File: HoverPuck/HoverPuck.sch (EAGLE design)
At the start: 14 parts, among them Q1 FDME, Q2 FDME, U1 EFM8BB1.QFN20, U2 TPS62177.DQC

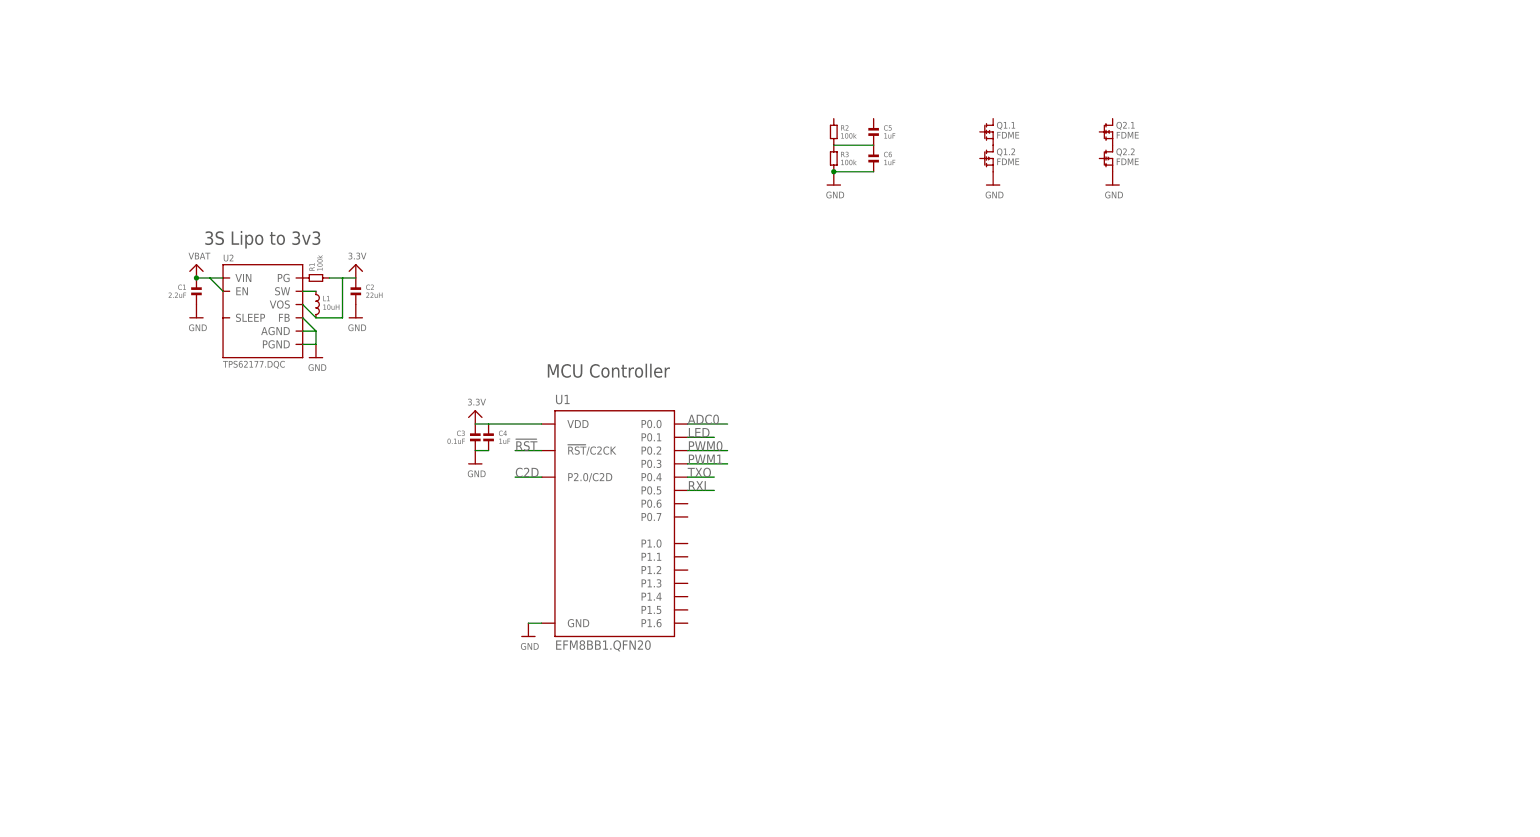
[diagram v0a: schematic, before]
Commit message: Schematic seems about done and layout of components looks promising Next step will be the actual routing
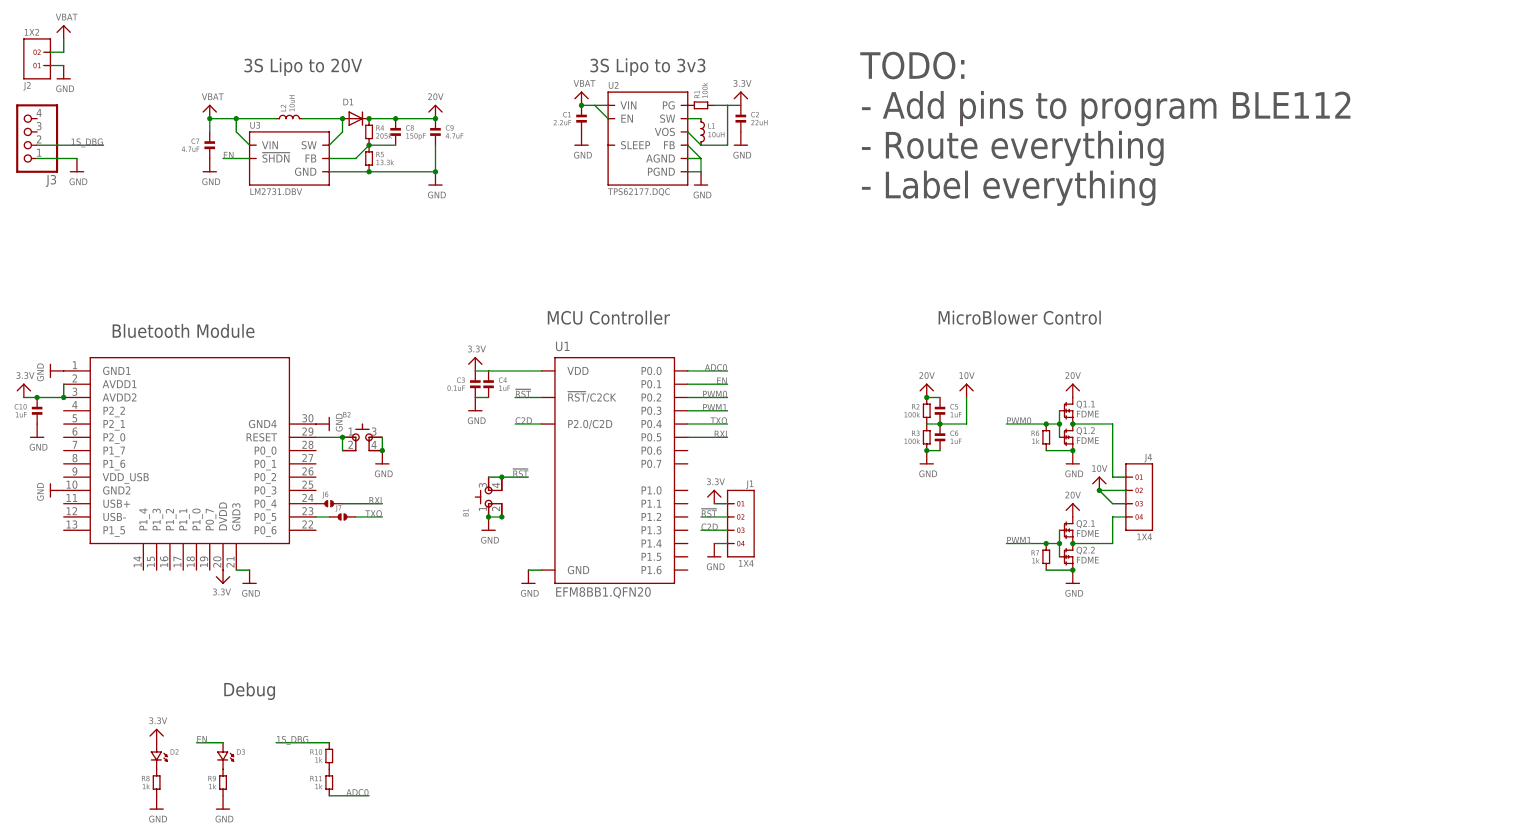
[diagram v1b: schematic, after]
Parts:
- added B1, B2: (no value), alps:SKSCLDE010
- added C10: 1uF, standardparts:CAPACITOR.0603
- added C7, C9: 4.7uF, standardparts:CAPACITOR.0805
- added C8: 150pF, standardparts:CAPACITOR.0603
- added D1: MBR0530T1G, microbuilder:DIODESOD-123
- added D2, D3: (no value), standardparts:LED.0603
- added J1, J4: 1X4, headers(2mm):1X4
- added J2: 1X2, headers.edge(.1in):1X2
- added J3: (no value), microbuilder:JST_4PIN
- added J6, J7: (no value), solderjumper:SOLDERJUMPER.2.SML.PASTE
- added L2: 10uH, bourns:INDUCTOR-SRN6045
- added R10, R11, R6, R7, R8, R9: 1k, standardparts:RESISTOR.0603
- added R4: 205k, standardparts:RESISTOR.0603
- added R5: 13.3k, standardparts:RESISTOR.0603
- added U3: LM2731.DBV, packages(ti):LM2731.DBV
- added U4: BLE112-A, SparkFun-RF:BLE112-A
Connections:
- removed net LED: U1.P0.1
- new net 10V: C5.2, C6.1, J4.2, J4.3, R2.2, R3.1
- new net 1S_DBG: J3.2, R10.1
- new net 20V: C5.1, C8.1, C9.1, D1.C, Q1.1.D, Q2.1.D, R2.1, R4.1
- new net EN: D2.1, D3.1, U1.P0.1, U3.!SHDN
- new net N$10: J6.1, U4.P0_4
- new net N$11: J7.1, U4.P0_5
- new net N$12: B2.1, B2.2, U4.RESET
- new net N$5: D1.A, L2.2, U3.SW
- new net N$7: C8.2, R4.2, R5.1, U3.FB
- new net N$8: D3.2, R9.1
- new net N$9: R10.2, R11.1
- net !RST: now also B1.3, B1.4, J1.2
- net 3.3V: now also C10.1, J1.1, U4.AVDD1, U4.AVDD2, U4.DVDD
- net ADC0: now also R11.2
- net C2D: now also J1.3
- net GND: now also B1.1, B1.2, B2.3, B2.4, C10.2, C7.2, C9.2, J1.4, J2.1, J3.1, R5.2, R6.2, R7.2, R8.2, R9.2, U3.GND, U4.GND1, U4.GND2, U4.GND3, U4.GND4
- net N$1: now also J4.1
- net N$2: now also J4.4
- net N$4: now also D2.2, R8.1; no longer C5.2, C6.1, R2.2, R3.1
- net PWM0: now also Q1.1.G, Q1.2.G, R6.1
- net PWM1: now also Q2.1.G, Q2.2.G, R7.1
- net RXI: now also J6.2
- net TXO: now also J7.2
- net VBAT: now also C7.1, J2.2, L2.1, U3.VIN
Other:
- note added: "3S Lipo to 20V"
- note added: "Bluetooth Module"
- note added: "Debug"
- note added: "MicroBlower Control"
- note added: "TODO: - Add pins to program BLE112 - Route everything - Label everything"
- moved on the sheet: C1, C2, C3, C4, C5, C6, L1, Q1.1, Q1.2, Q2.1, Q2.2, R1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

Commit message: Updated TODO list
Added more references on what signals to breakout for BLE112
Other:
- note added: "TODO: - Add pins to program BLE112 - Finish Routing - Label everything - Breakout Programming pins for BLE112 - https://github.com/slackhappy/ble112/blob/master/programming.md - http://www.inmojo.com/store/jeff-rowberg/item/ble112-bluetooth-low-energy-breakout/ - https://github.com/slackhappy/ble112/tree/master/serial_debug - Breakout Programming pins for EFM8BB1 - -"
- note removed: "TODO: - Add pins to program BLE112 - Route everything - Label everything"
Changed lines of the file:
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@@
 <text x="170.18" y="165.1" size="5.08" layer="97" ratio="15" align="top-left">TODO:
 - Add pins to program BLE112
-- Route everything
-- Label everything</text>
+- Finish Routing
+- Label everything
+- Breakout Programming pins for BLE112
+  - https://github.com/slackhappy/ble112/blob/master/programming.md
+  - http://www.inmojo.com/store/jeff-rowberg/item/ble112-bluetooth-low-energy-breakout/
+  - https://github.com/slackhappy/ble112/tree/master/serial_debug
+- Breakout Programming pins for EFM8BB1
+  -
+- </text>
 <text x="200.66" y="114.3" size="2.54" layer="97" ratio="15" align="center">MicroBlower Control</text>
 <text x="53.34" y="43.18" size="2.54" layer="97" ratio="15" align="center">Debug</text>

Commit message: Added single debugger connector
Replaced 1k resistors with resistor array
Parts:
- removed B2: (no value), alps:SKSCLDE010
- removed J1: 1X4, headers(2mm):1X4
- removed R8, R9: 1k, standardparts:RESISTOR.0603
- added D4: (no value), standardparts:LED.0603
- added RA1: (no value), resistorarray:RA-4.0603
- added U$38, U$39: 1X5, headers(.05in):1X5
- R10, R11, R6, R7: value 1k -> 10k
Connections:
- removed net !RST: B1.3, B1.4, J1.2, U1.!RST!/C2CK
- removed net C2D: J1.3, U1.P2.0/C2D
- removed net EN: D2.1, D3.1, U1.P0.1, U3.!SHDN
- removed net N$12: B2.1, B2.2, U4.RESET
- new net 20V_EN: RA1.2.2, U1.P0.1, U3.!SHDN
- new net BLE_!RST: RA1.4.1, U$38.4, U1.P0.7, U4.RESET
- new net BLE_DC: U$38.2, U4.P2_2
- new net BLE_DD: U$39.2, U4.P2_1
- new net EFM8_C2CK: B1.3, B1.4, U$39.3, U1.!RST!/C2CK
- new net EFM8_C2D: U$38.3, U1.P2.0/C2D
- new net STATUS: RA1.3.2, U1.P0.6
- net 3.3V: now also RA1.1.2, RA1.4.2, U$38.5, U$39.1; no longer J1.1
- net ADC0: now also R10.2, R11.1; no longer R11.2
- net GND: now also D2.2, D3.2, D4.2, R11.2, U$38.1, U$39.5; no longer B2.3, B2.4, J1.4, R8.2, R9.2
- net N$4: now also D2.1, RA1.1.1; no longer D2.2, R8.1
- net N$8: now also D3.1, RA1.2.1; no longer D3.2, R9.1
- net N$9: now also D4.1, RA1.3.1; no longer R10.2, R11.1
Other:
- note added: "TODO: - Optimize pin placement in EFM8 - Add testpoints everywhere - Complete routing"
- note removed: "TODO: - Add pins to program BLE112 - Finish Routing - Label everything - Breakout Programming pins for BLE112 - https://github.com/slackhappy/ble112/blob/master/programming.md - http://www.inmojo.com/store/jeff-rowberg/item/ble112-bluetooth-low-energy-breakout/ - https://github.com/slackhappy/ble112/tree/master/serial_debug - Breakout Programming pins for EFM8BB1 - -"
- moved on the sheet: B1, C10, C3, C4, C5, C6, D2, D3, J4, J6, J7, Q1.1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

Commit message: Completed v1 of HoverPuck PCB
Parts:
- added J1: (no value), solderjumper:SOLDERJUMPER.2.SML.PASTE
- added TP1, TP2, TP3, TP4: TPTP06R, testpad:TPTP06R
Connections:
- removed net N$9 (its old number): D4.1, RA1.3.1
- new net N$12: J1.1, U1.P0.1
- new net N$8: D4.1, RA1.1.1
- net 20V: now also TP2.TP
- net 20V_EN: now also U1.P0.0; no longer U1.P0.1
- net 3.3V: now also RA1.3.2, TP1.TP; no longer RA1.1.2
- net ADC0: now also J1.2; no longer U1.P0.0
- net BLE_!RST: now also RA1.3.1, U1.P1.0; no longer RA1.4.1, U1.P0.7
- net N$4: now also RA1.4.1; no longer RA1.1.1
- net PWM0: now also Q2.1.G, Q2.2.G, R7.1, TP4.TP, U1.P0.3; no longer Q1.1.G, Q1.2.G, R6.1, U1.P0.2
- net PWM1: now also Q1.1.G, Q1.2.G, R6.1, TP3.TP, U1.P0.6; no longer Q2.1.G, Q2.2.G, R7.1, U1.P0.3
- net STATUS: now also RA1.1.2, U1.P0.7; no longer RA1.3.2, U1.P0.6
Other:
- note added: "AnomalousMaker.com"
- note added: "Author: Cruz Monrreal II"
- note removed: "TODO: - Optimize pin placement in EFM8 - Add testpoints everywhere - Complete routing"
- moved on the sheet: C2, RA1.1, RA1.3, RA1.4

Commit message: Started v2 of the HoverPuck. Changed driver circuit, and moving things around. New driver circuit still needs to be confirmed functional.
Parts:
- removed J3: (no value), microbuilder:JST_4PIN
- removed J4: 1X4, headers(2mm):1X4
- removed Q1, Q2: FDME, fairchild:FDME
- removed R2, R3: 100k, standardparts:RESISTOR.0603
- removed R6, R7: 10k, standardparts:RESISTOR.0603
- added C11, C12, C13, C14: 0.1uF, standardparts:CAPACITOR.0603
- added MB0, MB1: 1X2, headers.edge(.1in):1X2
- added TP5, TP6: TPTP06R, testpad:TPTP06R
- added U5, U6: (no value), packages(ti):DRV8800.RTY
- C5, C6: value 1uF -> 0.1uF
- J2: value 1X2 -> 1X4; device headers.edge(.1in):1X2 -> headers.edge(.1in):1X4
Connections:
- removed net 10V: C5.2, C6.1, J4.2, J4.3, R2.2, R3.1
- new net 12V: C12.1, C13.1, C14.1, C5.1, U5.VMOT, U6.VMOT
- new net EN_20V: U5.!SLEEP, U6.!SLEEP
- new net N$13: MB0.1, U5.OUT+
- new net N$14: MB0.2, U5.OUT-
- new net N$15: MB1.1, U6.OUT+
- new net N$16: MB1.2, U6.OUT-
- new net N$17: C6.1, U5.CP1
- new net N$18: C6.2, U5.CP2
- new net N$19: C11.2, U6.CP2
- new net N$20: C11.1, U6.CP1
- net 1S_DBG: now also J2.3; no longer J3.2
- net 20V: no longer C5.1, Q1.1.D, Q2.1.D, R2.1
- net 20V_EN: now also TP5.TP
- net 3.3V: now also U5.ENABLE, U5.MODE, U6.ENABLE, U6.MODE
- net GND: now also C13.2, C14.2, J2.4, TP6.TP, U5.GND, U5.SENSE, U6.GND, U6.SENSE; no longer C6.2, J2.1, J3.1, Q1.2.S, Q2.2.S, R3.2, R6.2, R7.2
- net N$1: now also C12.2, U6.VCP; no longer J4.1, Q1.1.S, Q1.2.D
- net N$2: now also C5.2, U5.VCP; no longer J4.4, Q2.1.S, Q2.2.D
- net PWM0: now also TP3.TP, U5.PHASE; no longer Q2.1.G, Q2.2.G, R7.1, TP4.TP
- net PWM1: now also TP4.TP, U6.PHASE; no longer Q1.1.G, Q1.2.G, R6.1, TP3.TP
- net VBAT: now also J2.1; no longer J2.2
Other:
- moved on the sheet: C5, C6, U$38, U$39
